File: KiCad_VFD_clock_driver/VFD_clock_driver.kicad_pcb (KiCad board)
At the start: 2 copper layers, 61 parts, among them J1 Barrel_Jack, J2 SWD, J3 Multiplexer, J4 Segments, SW1 RESET, SW2 SELECT, SW3 PLUS, SW4 MINUS, U1 DS3231M, U2 SX1308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

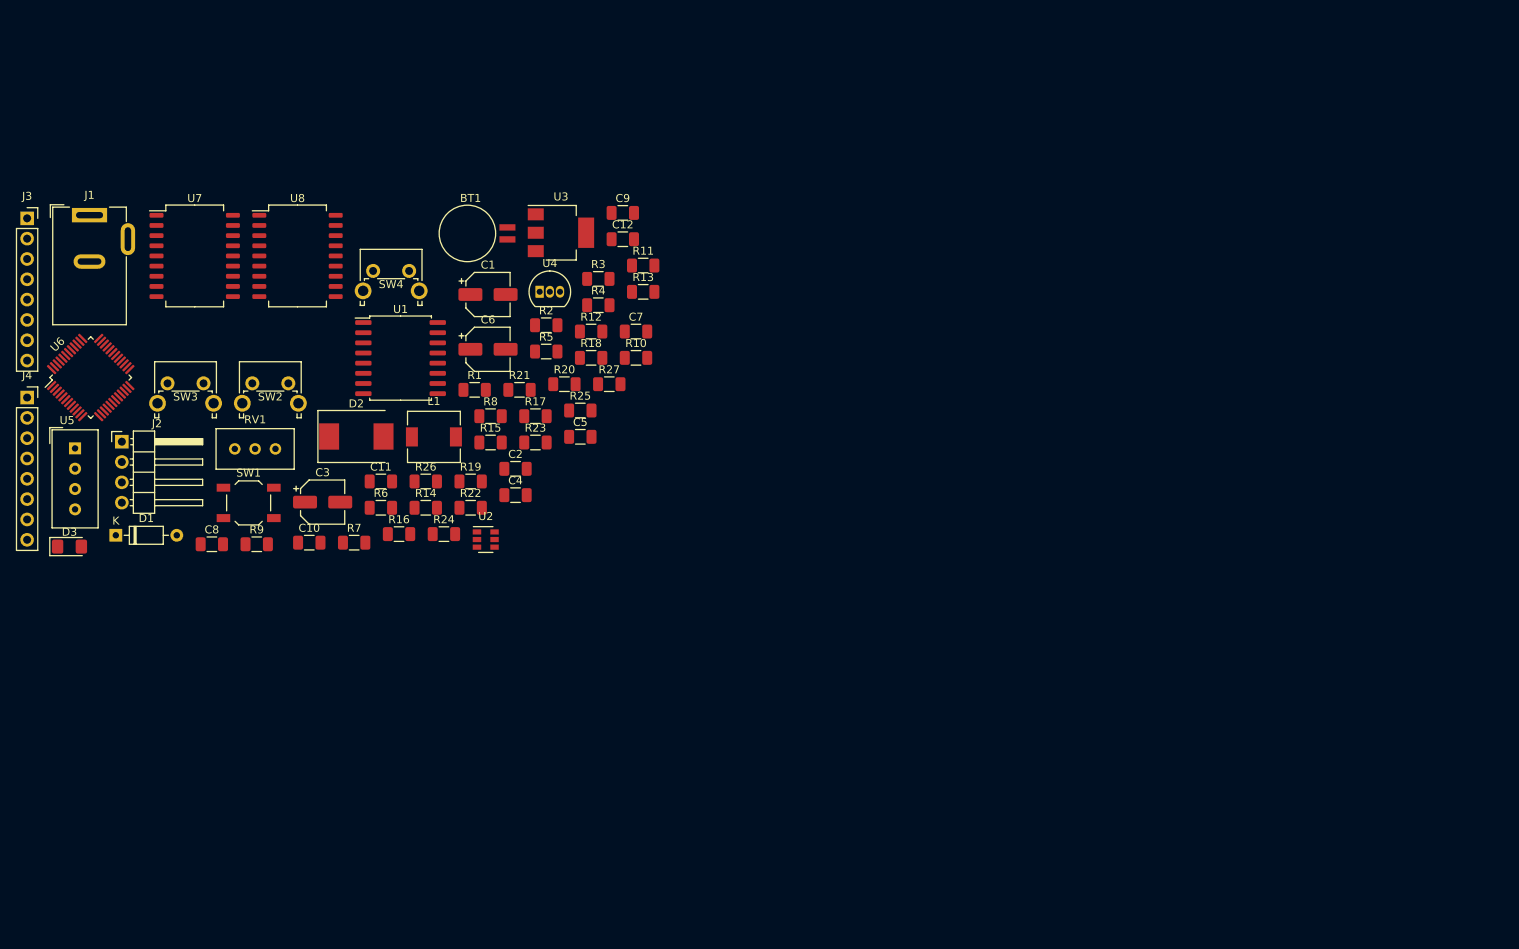
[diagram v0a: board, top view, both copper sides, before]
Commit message: Buzzer and additional inputs
+ added buzzer with circuitry
+ SQW and UART connected to MCU
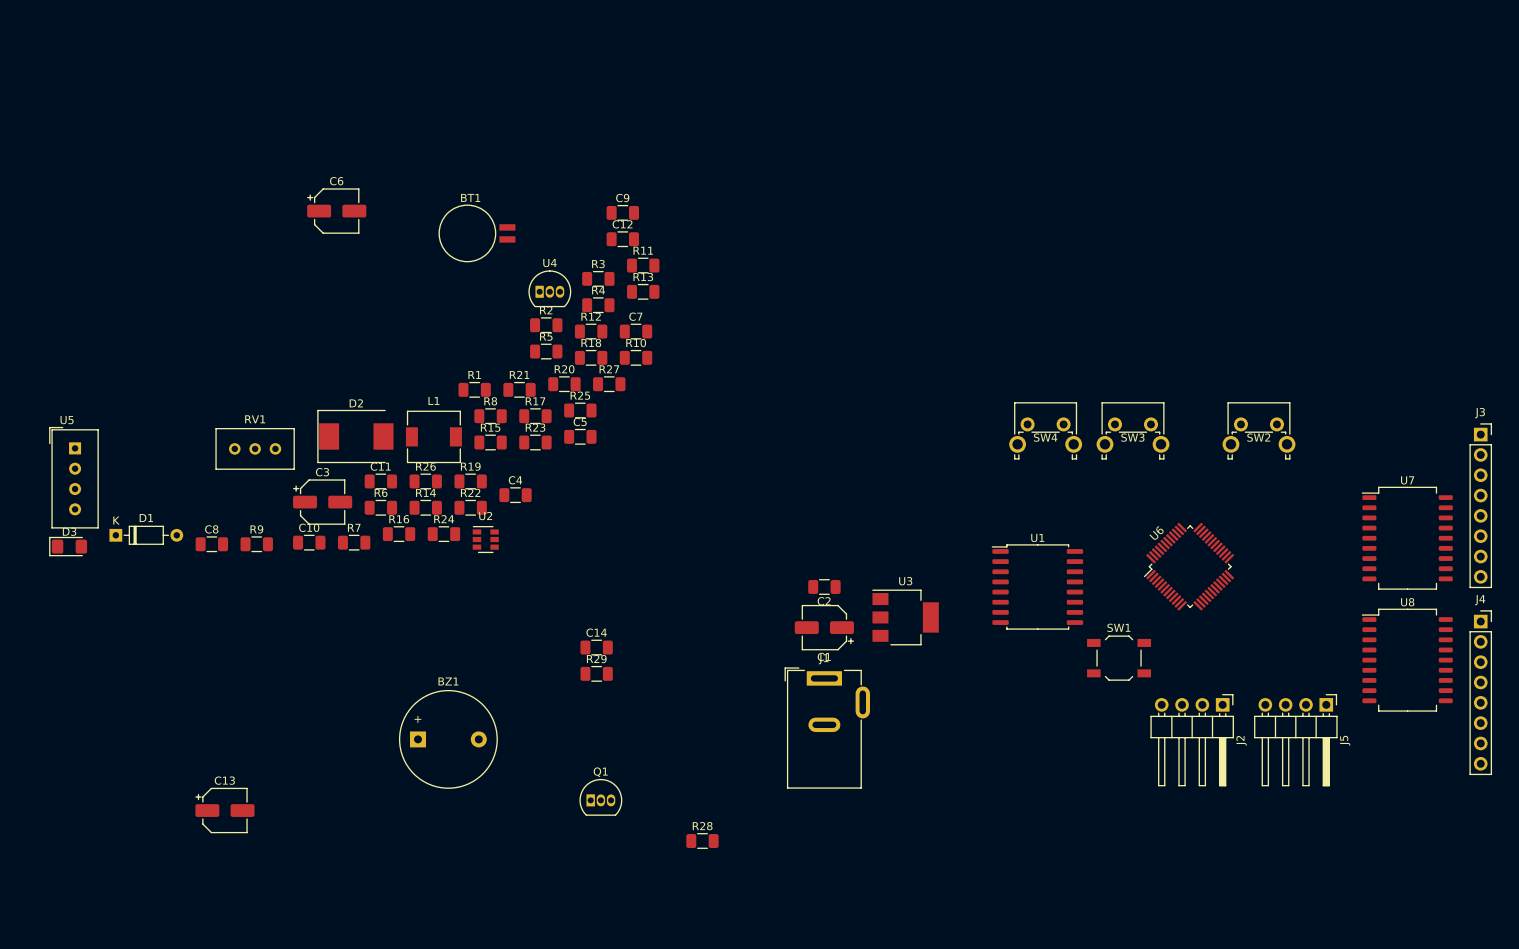
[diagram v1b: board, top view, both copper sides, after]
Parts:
- added BZ1: Buzzer, Buzzer_Beeper:Buzzer_12x9.5RM7.6, F.Cu at (105.4, 115.6)
- added C13: 47uF, Capacitor_SMD:CP_Elec_5x4.4, F.Cu at (81.3, 124.5)
- added C14: 100nF, Capacitor_SMD:C_1206_3216Metric, F.Cu at (127.7, 104.1)
- added J5: UART, Connector_PinHeader_2.54mm:PinHeader_1x04_P2.54mm_Horizontal, F.Cu at (218.9, 111.3)
- added Q1: BC547, Package_TO_SOT_THT:TO-92_Inline, F.Cu at (127.0, 123.2)
- added R28: 1K, Resistor_SMD:R_1206_3216Metric, F.Cu at (141.0, 128.3)
- added R29: 10K, Resistor_SMD:R_1206_3216Metric, F.Cu at (127.7, 107.4)
- moved J4 183.8 mm to (238.3, 100.8)
- moved J3 183.7 mm to (238.3, 77.5)
- moved U7 155.7 mm to (229.1, 90.4)
- moved U8 147.7 mm to (229.1, 105.7)
- moved J2 141.5 mm to (206.0, 111.3), turned to 270 degrees
- moved U6 139.4 mm to (201.9, 94.0)
- moved SW2 123.7 mm to (208.3, 76.2)
- moved SW3 118.5 mm to (192.5, 76.2)
- moved SW1 110.5 mm to (193.0, 105.4)
- moved J1 108.6 mm to (156.2, 108.0)
- moved U1 84.6 mm to (182.9, 96.5)
- moved SW4 84.0 mm to (181.6, 76.2)
- moved U3 64.6 mm to (166.4, 100.3)
- moved C1 59.2 mm to (156.2, 101.6), turned to 180 degrees
- moved C2 41.3 mm to (156.2, 96.5), turned to 180 degrees
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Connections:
- net Net-(C1-Pad1) renamed /VIN
- U6 pad 29: (no net) -> /BUZZER
- U6 pad 30: (no net) -> Net-(J5-Pad3)
- U6 pad 31: (no net) -> Net-(J5-Pad2)
- U6 pad 5: (no net) -> /SQW

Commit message: Power supply section in PCB
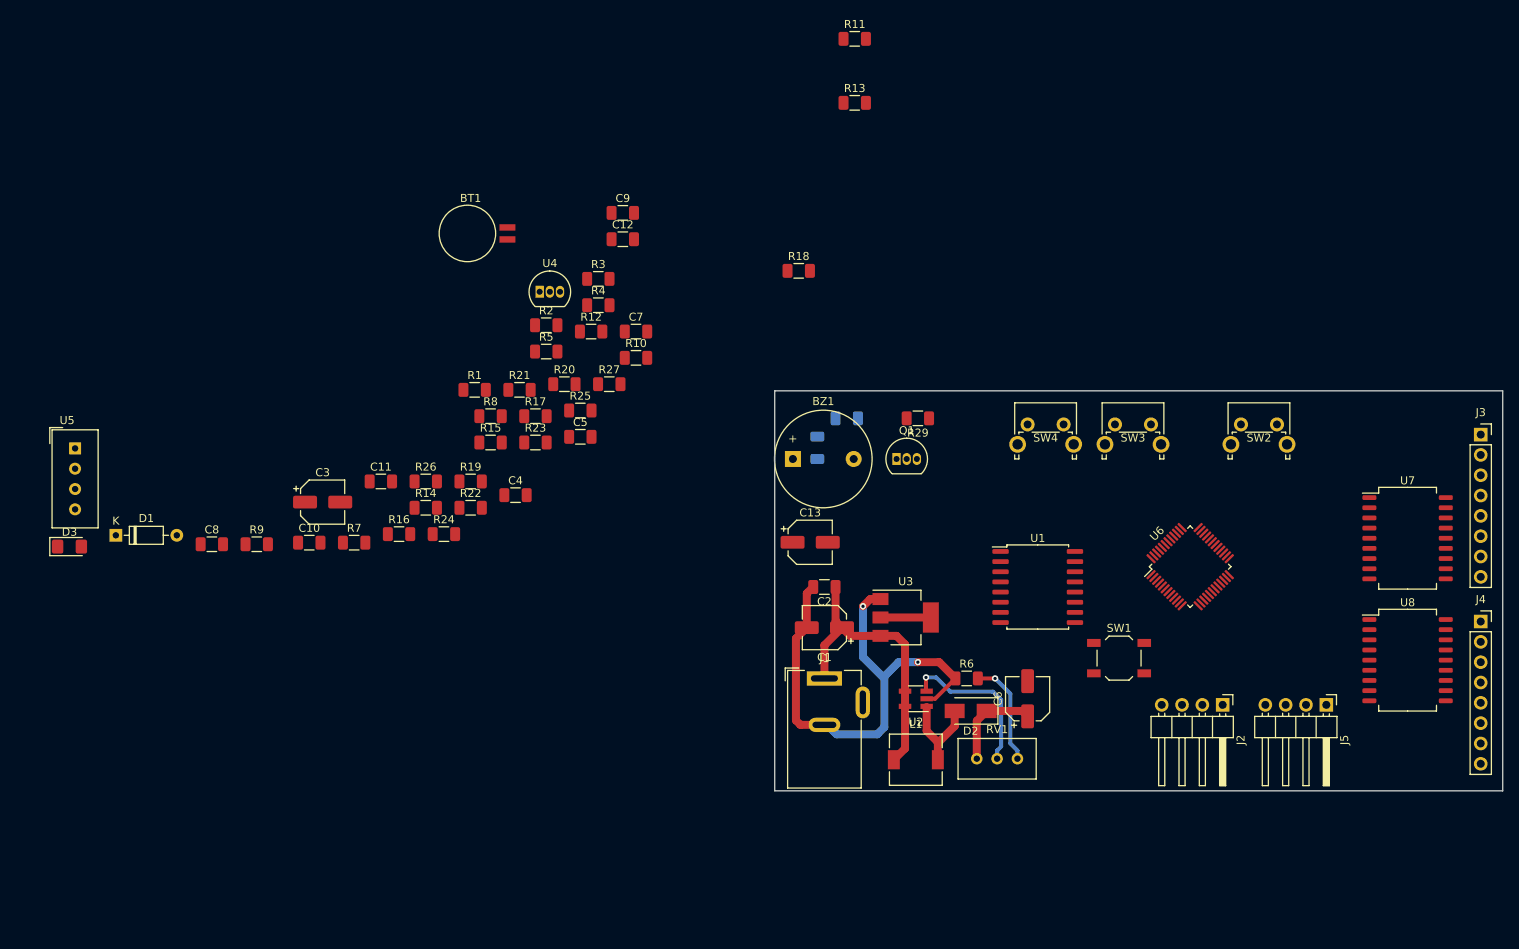
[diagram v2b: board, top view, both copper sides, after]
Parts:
- C14, R28: moved to B.Cu
- D2: footprint Diode_SMD:D_SMC -> Diode_SMD:D_SMA
- U2: footprint Package_TO_SOT_SMD:SOT-23-6 -> Package_TO_SOT_SMD:SOT-23-5_HandSoldering
- moved C6 105.7 mm to (181.6, 110.5), turned to 90 degrees
- moved RV1 100.5 mm to (180.3, 118.0)
- moved D2 84.1 mm to (174.5, 112.0), turned to 180 degrees
- moved C13 80.5 mm to (154.4, 90.9)
- moved R6 76.3 mm to (174.0, 108.0)
- moved L1 72.5 mm to (167.6, 118.1)
- moved BZ1 58.5 mm to (152.3, 80.5)
- moved U2 57.3 mm to (167.6, 110.5), turned to 180 degrees
- moved Q1 57.3 mm to (165.2, 80.5)
- moved R29 51.3 mm to (167.9, 75.4), turned to 180 degrees
- moved R28 51.2 mm to (155.3, 79.1), turned to 90 degrees
- moved C14 42.4 mm to (159.0, 75.4), turned to 180 degrees
- moved R11 38.8 mm to (160.0, 28.0)
- moved R13 35.5 mm to (160.0, 36.0)
- moved R18 28.1 mm to (153.0, 57.0)
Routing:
- net GND: track 0.00 -> 63.7 mm, vias 0 -> 2
- net /VIN: track 0.00 -> 36.4 mm
- net Net-(RV1-Pad2): track 0.00 -> 19.9 mm, vias 0 -> 1
- net Net-(R6-Pad2): track 0.00 -> 13.3 mm, vias 0 -> 1
- net Net-(D2-Pad2): track 0.00 -> 12.0 mm
- net /HV: track 0.00 -> 11.9 mm
- net +3V3: track 0.00 -> 6.30 mm
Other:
- board outline added: 91 x 50 mm

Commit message: Final PCB routing
+ updated gitignore with some unnecessary KiCad files
+ final component placement on BCB
+ final routing on PCB
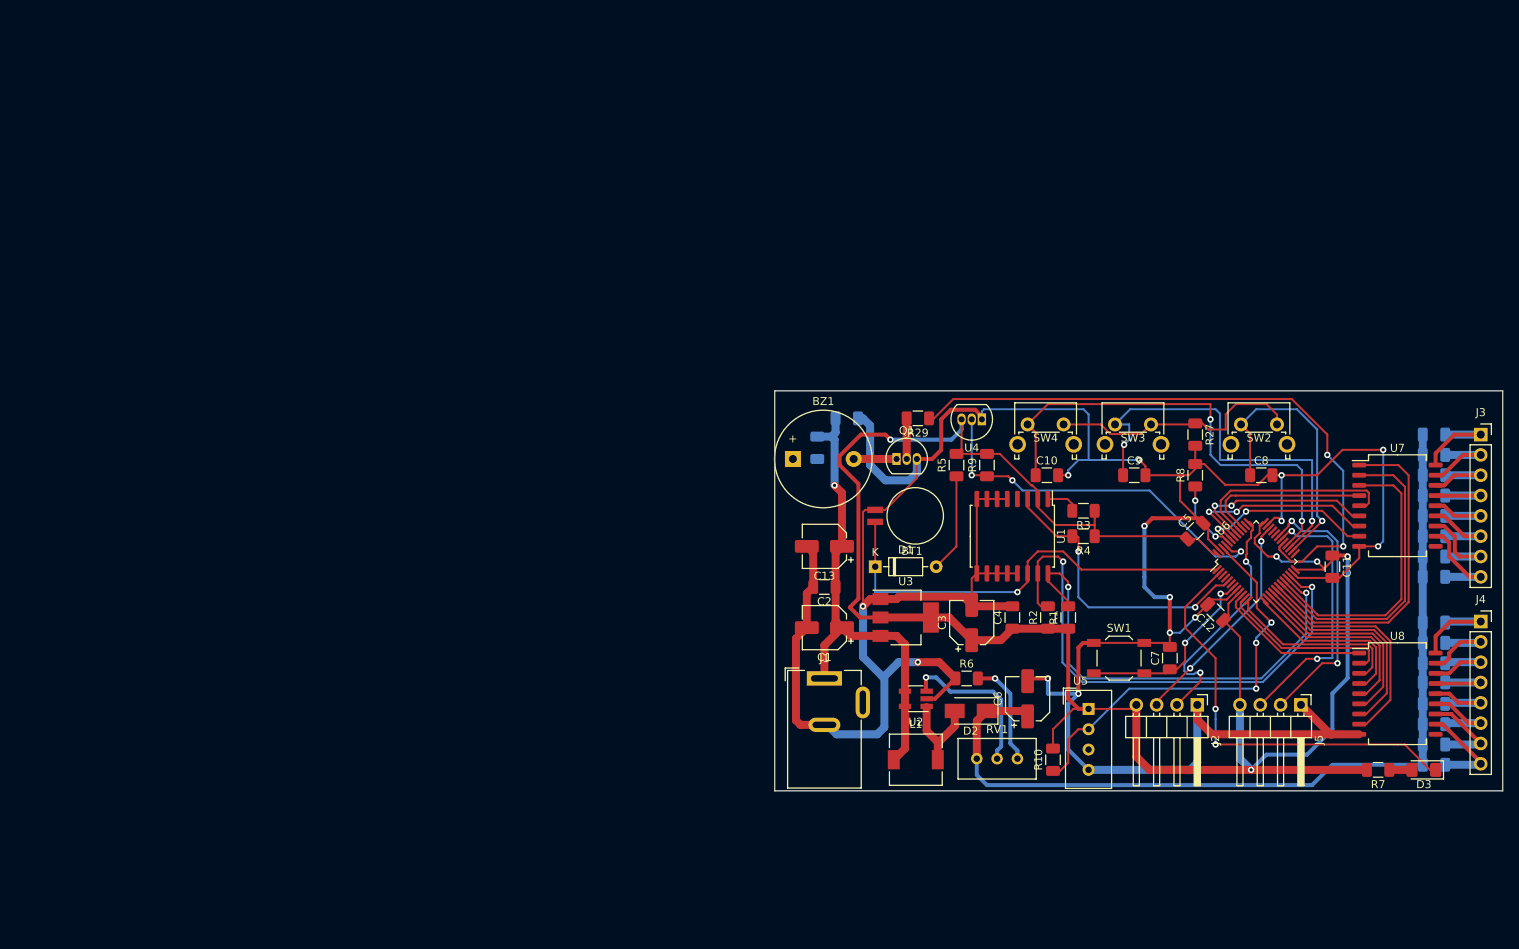
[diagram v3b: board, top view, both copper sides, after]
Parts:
- R11, R12, R13, R14, R15, R16, R17, R18, R19, R20, R21, R22, R23, R24, R25, R26: moved to B.Cu
- moved D3 171.6 mm to (231.1, 119.4), turned to 180 degrees
- moved C8 131.5 mm to (210.8, 82.5)
- moved R7 131.1 mm to (225.4, 119.4), turned to 180 degrees
- moved R26 130.9 mm to (232.4, 118.7), turned to 180 degrees
- moved U5 130.8 mm to (189.2, 111.8)
- moved R16 130.4 mm to (232.4, 106.0), turned to 180 degrees
- moved R14 127.2 mm to (232.4, 103.5), turned to 180 degrees
- moved R24 126.5 mm to (232.4, 116.2), turned to 180 degrees
- moved R22 123.4 mm to (232.4, 113.7), turned to 180 degrees
- moved R19 120.5 mm to (232.4, 87.6), turned to 180 degrees
- moved C11 119.4 mm to (219.7, 94.0), turned to 270 degrees
- moved R15 118.0 mm to (232.4, 82.5), turned to 180 degrees
- moved R20 115.8 mm to (232.4, 111.1), turned to 180 degrees
- moved R21 115.8 mm to (232.4, 90.2), turned to 180 degrees
- moved R23 113.2 mm to (232.4, 92.7), turned to 180 degrees
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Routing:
- net GND: track 63.7 -> 397.8 mm, vias 2 -> 14
- net +3V3: track 6.30 -> 256.5 mm, vias 0 -> 5
- net /HV: track 11.9 -> 112.5 mm
- net /BUZZER: track 0.00 -> 78.0 mm, vias 0 -> 2
- net /SDA: track 0.00 -> 66.9 mm, vias 0 -> 2
- net /SCL: track 0.00 -> 59.5 mm, vias 0 -> 2
- net /BUTTON_MINUS: track 0.00 -> 59.4 mm, vias 0 -> 2
- net /VBAT: track 0.00 -> 56.0 mm, vias 0 -> 1
- net Net-(D3-Pad1): track 0.00 -> 53.7 mm, vias 0 -> 2
- net /DHT_interface: track 0.00 -> 52.3 mm, vias 0 -> 3
- net /BUTTON_PLUS: track 0.00 -> 52.0 mm, vias 0 -> 2
- net /OneWire: track 0.00 -> 47.4 mm, vias 0 -> 3
- net /L1: track 0.00 -> 41.8 mm
- net /L2: track 0.00 -> 38.8 mm
- net /SQW: track 0.00 -> 37.1 mm, vias 0 -> 2
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
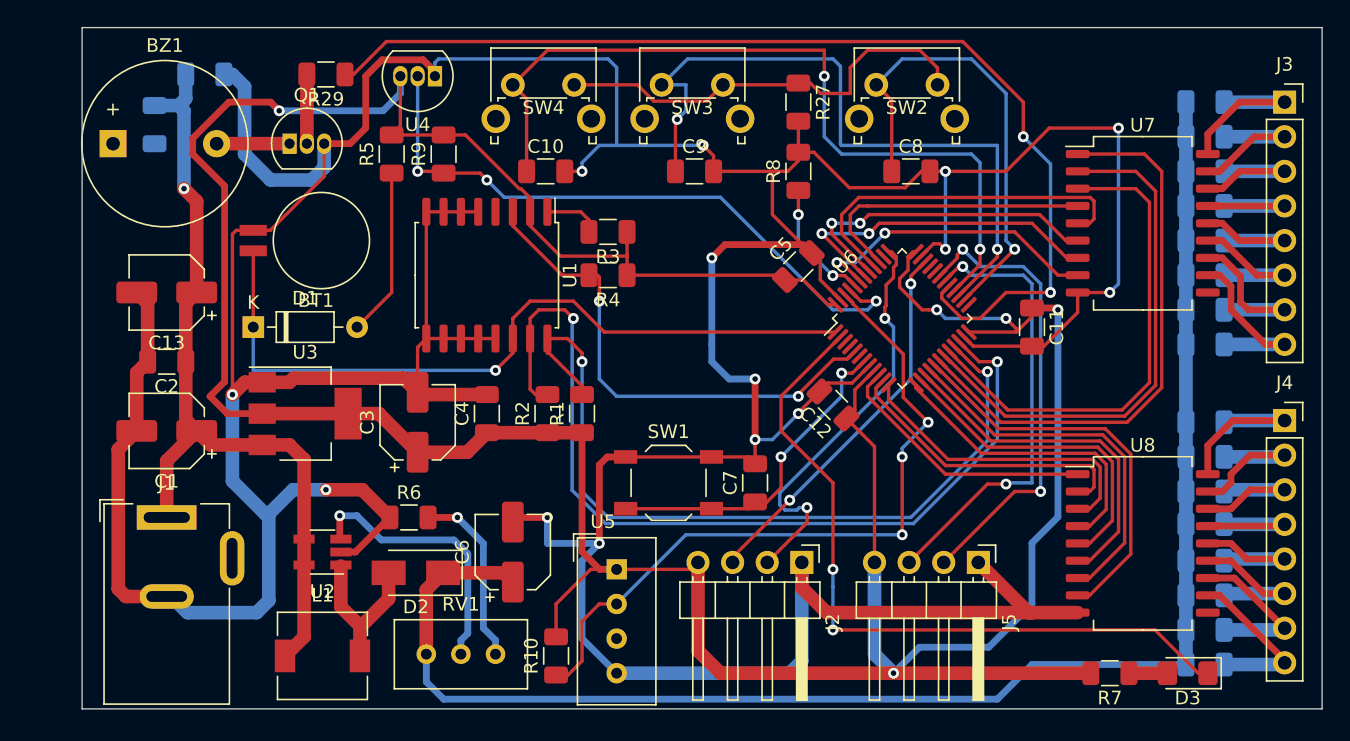
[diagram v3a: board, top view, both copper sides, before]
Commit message: Silkscreen and planes on PCB
+ final silkscreen on PCB
+ small routing and component location tweaks
+ GND planes on PCB
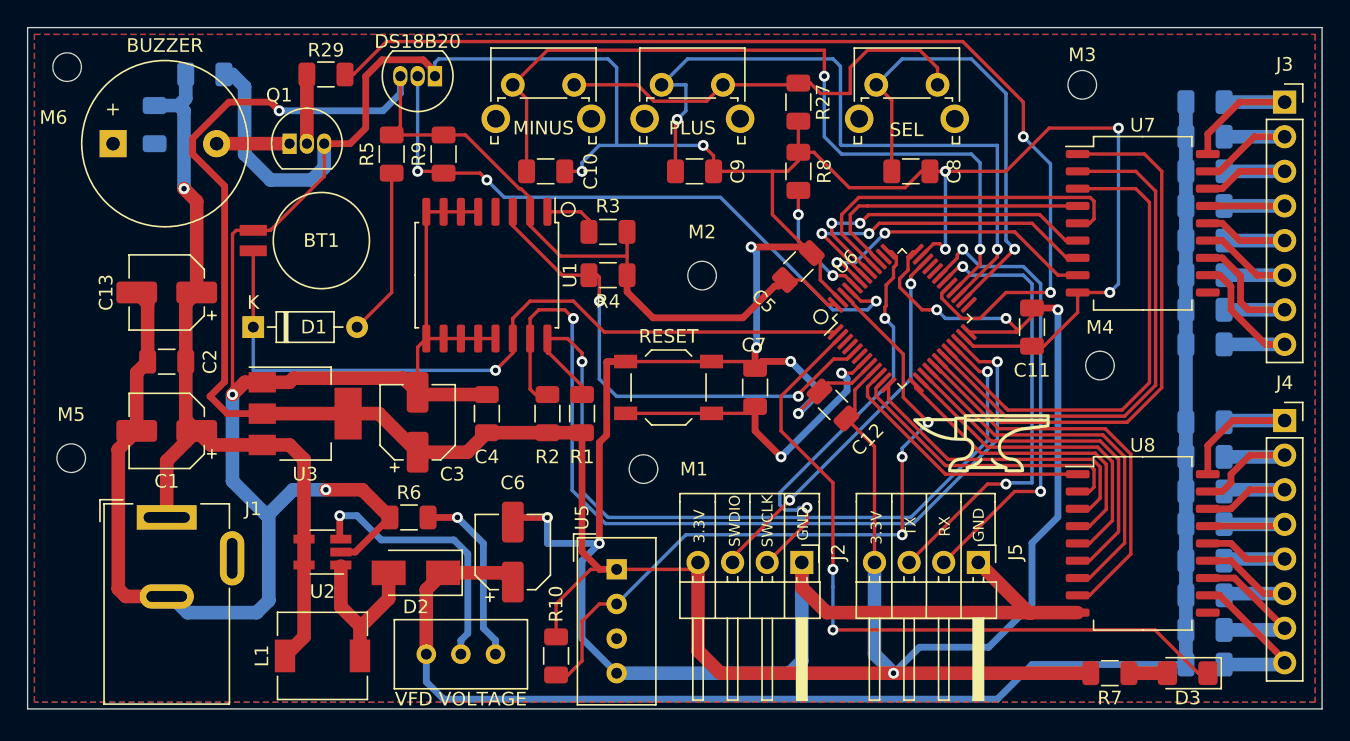
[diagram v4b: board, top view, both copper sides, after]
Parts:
- removed SW1: RESET, Button_Switch_SMD:SW_SPST_TL3342
- added G***: LOGO, WK_lib:Anvil_10x10mm, F.Cu at (216.0, 102.5)
- added G***: LOGO, WK_lib:Anvil_10x10mm, B.Cu at (176.0, 86.0)
- added M1: MountingHole_2.1mm, MountingHole:MountingHole_2.1mm, F.Cu at (191.2, 104.4)
- added M2: MountingHole_2.1mm, MountingHole:MountingHole_2.1mm, F.Cu at (195.5, 90.2)
- added M3: MountingHole_2.1mm, MountingHole:MountingHole_2.1mm, F.Cu at (223.4, 76.2)
- added M4: MountingHole_2.1mm, MountingHole:MountingHole_2.1mm, F.Cu at (224.7, 96.8)
- added M5: MountingHole_2.1mm, MountingHole:MountingHole_2.1mm, F.Cu at (149.2, 103.6)
- added M6: MountingHole_2.1mm, MountingHole:MountingHole_2.1mm, F.Cu at (148.9, 74.9)
- added RESET: RESET, Button_Switch_SMD:SW_SPST_TL3342, F.Cu at (193.0, 98.4)
- VFD VOLTAGE: renamed from RV1
- moved C7 7.00 mm to (199.4, 98.4)
- renumbered BZ1 to BUZZER, U4 to DS18B20, SW4 to MINUS, SW3 to PLUS, SW2 to SEL
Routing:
- net +3V3: track 256.5 -> 260.0 mm
- added copper zone on B.Cu, net GND
- added copper zone on F.Cu, net GND
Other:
- board size 91 x 50 mm -> 95 x 50 mm
- board text added: "3.3V"
- board text added: "GND"
- board text added: "RX"
- board text added: "SWCLK"
- board text added: "SWDIO"
- board text added: "TX"
- board text added: "VFD clock driver"
